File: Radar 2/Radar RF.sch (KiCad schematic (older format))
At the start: 140 parts, among them U10 Check_Point, U11 Check_Point, U12 TLV172, U13 5400BL15B050E, U14 Check_Point, U15 LT6232, U16 Check_Point, U17 HMC431LP4, U18 TRF37A75, U19 PAT1220-C-6DB, U20 SKY65404, U21 TQP5523, U22 SMA_Connector, U23 MITERED_BEND, U24 Check_Point, U26 Check_Point, U27 PAT1220-C-6DB, U28 MITERED_BEND, U29 Directional_Coupler, U30 SMA_Connector, U34 Check_Point, U36 Check_Point, U42 MITERED_BEND, U43 MITERED_BEND, U44 MITERED_BEND, U46 Check_Point, U5 Check_Point, U6 SG-210STF, U7 5400BL15B050E, U8 ADF4158, U9 ADL5801

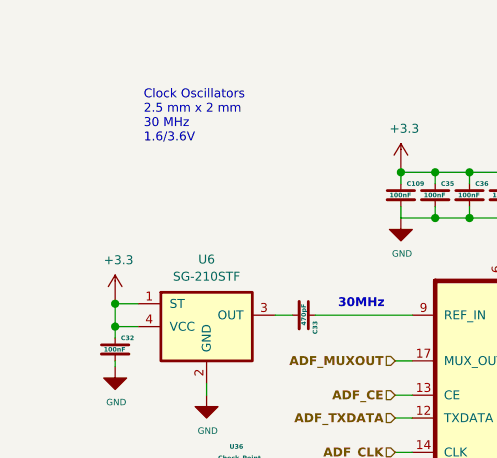
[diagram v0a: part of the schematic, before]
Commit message: Added datasheet for clock oscillator
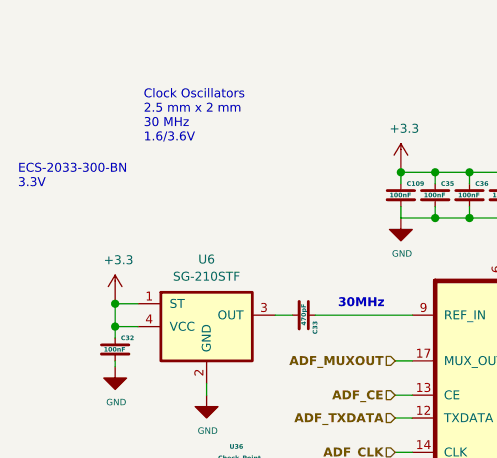
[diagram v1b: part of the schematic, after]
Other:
- note added: "ECS-2033-300-BN\n3.3V"
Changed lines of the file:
@@
 Text Notes 13500 1100 0    39   ~ 0
 CMX901QT8\nRF Amplifier 1W RF Power Amplifier\n130 MHz to 950 MHz\nGain 32dB\n6/2.5V\n
+Text Notes 750  1250 0    39   ~ 0
+ECS-2033-300-BN\n3.3V
 $EndSCHEMATC

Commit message: Minor changes in schematic
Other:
- note added: "Change this to 3 volt\nThis is tuning voltage"
- note added: "TLV172 not required as tunign volatge is upto 3 volt only"
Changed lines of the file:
@@
 Text Notes 750  1250 0    39   ~ 0
 ECS-2033-300-BN\n3.3V
+Text Notes 4350 1200 0    39   Italic 0
+Change this to 3 volt\nThis is tuning voltage
+Wire Notes Line
+	4350 1000 5050 1000
+Wire Notes Line
+	5050 1000 5050 1300
+Wire Notes Line
+	5050 1300 4350 1300
+Wire Notes Line
+	4350 1300 4350 1000
+Wire Notes Line
+	5150 900  7100 900
+Wire Notes Line
+	7100 900  7100 3000
+Wire Notes Line
+	7100 3000 5200 3000
+Wire Notes Line
+	5200 3000 5200 900
+Text Notes 5250 850  0    39   ~ 0
+TLV172 not required as tunign volatge is upto 3 volt only
+Wire Notes Line
+	9900 1900 10750 1900
+Wire Notes Line
+	10750 1900 10750 3200
+Wire Notes Line
+	10750 3200 9900 3200
+Wire Notes Line
+	9900 3200 9900 1900
+Wire Notes Line
+	7550 1550 8400 1550
+Wire Notes Line
+	8400 1550 8400 2500
+Wire Notes Line
+	8400 2500 7550 2500
+Wire Notes Line
+	7550 2500 7550 1550
+Wire Notes Line
+	11200 1700 12650 1700
+Wire Notes Line
+	12650 1700 12650 3050
+Wire Notes Line
+	12650 3050 11200 3050
+Wire Notes Line
+	11200 3050 11200 1700
+Wire Notes Line
+	11050 5400 12000 5400
+Wire Notes Line
+	12000 5400 12000 6350
+Wire Notes Line
+	12000 6350 11050 6350
+Wire Notes Line
+	11050 6350 11050 5400
+Wire Notes Line
+	7800 5700 8500 5700
+Wire Notes Line
+	8500 5700 8500 6400
+Wire Notes Line
+	8500 6400 7800 6400
+Wire Notes Line
+	7800 6400 7800 5700
+Wire Notes Line
+	2500 5600 3250 5600
+Wire Notes Line
+	3250 5600 3250 6350
+Wire Notes Line
+	3250 6350 2500 6350
+Wire Notes Line
+	2500 6350 2500 5600
 $EndSCHEMATC

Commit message: Modified for SubGHz. Added all datasheet for reference.
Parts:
- removed C59, C85, C87, C88: 100nF, Footprints:SMD_0402, symbol Radar-v2-rescue:Capacitor-Capacitor-Radar-RF-rescue-Radar-v2-rescue
- removed C82, C90: 1nF, Footprints:SMD_0402, symbol Radar-v2-rescue:Capacitor-Capacitor-Radar-RF-rescue-Radar-v2-rescue
- removed C89: 10uF, Footprints:SMD_0603, symbol Radar-v2-rescue:Capacitor-Capacitor-Radar-RF-rescue-Radar-v2-rescue
- removed L8: BLM18PG181SN1D, Footprints:SMD_0603, symbol Radar-v2-rescue:Ferrite_Bead-Ferrite_Bead-Radar-RF-rescue-Radar-v2-rescue
- removed R35: 0, Footprints:SMD_0402, symbol Radar-v2-rescue:Resistor-Resistor-Radar-RF-rescue-Radar-v2-rescue
- removed R36, R37: 4.7K, Footprints:SMD_0402, symbol Radar-v2-rescue:Resistor-Resistor-Radar-RF-rescue-Radar-v2-rescue
- removed R38: 100K, Footprints:SMD_0402, symbol Radar-v2-rescue:Resistor-Resistor-Radar-RF-rescue-Radar-v2-rescue
- removed R56: 1K, Footprints:SMD_0402, symbol Radar-v2-rescue:Resistor-Resistor-Radar-RF-rescue-Radar-v2-rescue
- removed R57: 0 to 27, Footprints:SMD_0402, symbol Radar-v2-rescue:Resistor-Resistor-Radar-RF-rescue-Radar-v2-rescue
- removed R58: 30K, Footprints:SMD_0402, symbol Radar-v2-rescue:Resistor-Resistor-Radar-RF-rescue-Radar-v2-rescue
- removed R75: DNP, Footprints:SMD_0402, symbol Radar-v2-rescue:Resistor-Resistor-Radar-RF-rescue-Radar-v2-rescue
- removed R76: 100, Footprints:SMD_0402, symbol Radar-v2-rescue:Resistor-Resistor-Radar-RF-rescue-Radar-v2-rescue
- removed U11, U24: Check_Point, Footprints:SolderPad_1_1.5mm_SMD_Circle, symbol Radar-v2-rescue:SolderPad_1_Circle-SolderPad_1_Circle
- removed U12: TLV172, Footprints:SC70_5, symbol Radar-v2-rescue:TLV172-TLV172-Radar-RF-rescue-Radar-v2-rescue
- removed U13, U7: 5400BL15B050E, Footprints:Balun_5400BL15B050E, symbol Radar-v2-rescue:5400BL15B050E-Balun-Radar-RF-rescue-Radar-v2-rescue
- removed U19: PAT1220-C-6DB, Footprints:PAT1220_6dB, symbol Radar-v2-rescue:ATTENUATOR_3Pin-ATTENUATOR_3Pin-Radar-RF-rescue-Radar-v2-rescue
- removed U20: SKY65404, Footprints:SKY65404_31, symbol Radar-v2-rescue:SKY65404-SKY65404-Radar-RF-rescue-Radar-v2-rescue
- removed U21: TQP5523, Footprints:QFN20_4x4mm_P0.5mm_1EXP_2.5x2.5mm, symbol Radar-v2-rescue:TQP5523-TQP5523-Radar-RF-rescue-Radar-v2-rescue
- added C? (x7): DNP, Footprints:SMD_0402, symbol Radar-v2-rescue:Capacitor-Capacitor-Radar-RF-rescue-Radar-v2-rescue
- added C? (x3): 1uF, Footprints:SMD_0402, symbol Radar-v2-rescue:Capacitor-Capacitor-Radar-RF-rescue-Radar-v2-rescue
- added C?: 4.7uF, Footprints:SMD_0402, symbol Radar-v2-rescue:Capacitor-Capacitor-Radar-RF-rescue-Radar-v2-rescue
- added C? (x2): 10nF, Footprints:SMD_0402, symbol Radar-v2-rescue:Capacitor-Capacitor-Radar-RF-rescue-Radar-v2-rescue
- added C?: 100pF, Footprints:SMD_0402, symbol Radar-v2-rescue:Capacitor-Capacitor-Radar-RF-rescue-Radar-v2-rescue
- added C?: 4.7pF, Footprints:SMD_0402, symbol Radar-v2-rescue:Capacitor-Capacitor-Radar-RF-rescue-Radar-v2-rescue
- added C?: 18pF, Footprints:SMD_0402, symbol Radar-v2-rescue:Capacitor-Capacitor-Radar-RF-rescue-Radar-v2-rescue
- added C?: 5.6pF, Footprints:SMD_0402, symbol Radar-v2-rescue:Capacitor-Capacitor-Radar-RF-rescue-Radar-v2-rescue
- added C?: 1nF, Footprints:SMD_0402, symbol Radar-v2-rescue:Capacitor-Capacitor-Radar-RF-rescue-Radar-v2-rescue
- added L? (x2): 27nH, Footprints:SMD_0603, symbol Radar-v2-rescue:Ferrite_Bead-Ferrite_Bead-Radar-RF-rescue-Radar-v2-rescue
- added L?: 16nH, Footprints:SMD_0603, symbol Radar-v2-rescue:Ferrite_Bead-Ferrite_Bead-Radar-RF-rescue-Radar-v2-rescue
- added L?: 3.6nH, Footprints:SMD_0603, symbol Radar-v2-rescue:Ferrite_Bead-Ferrite_Bead-Radar-RF-rescue-Radar-v2-rescue
- added L?: 43nH, Footprints:SMD_0603, symbol Radar-v2-rescue:Ferrite_Bead-Ferrite_Bead-Radar-RF-rescue-Radar-v2-rescue
- added R? (x2): DNP, Footprints:SMD_0402, symbol Radar-v2-rescue:Resistor-Resistor-Radar-RF-rescue-Radar-v2-rescue
- added R? (x3): 68K, Footprints:SMD_0402, symbol Radar-v2-rescue:Resistor-Resistor-Radar-RF-rescue-Radar-v2-rescue
- added R?: 47K, Footprints:SMD_0402, symbol Radar-v2-rescue:Resistor-Resistor-Radar-RF-rescue-Radar-v2-rescue
- added R?: 100K, Footprints:SMD_0402, symbol Radar-v2-rescue:Resistor-Resistor-Radar-RF-rescue-Radar-v2-rescue
- added R?: 39K, Footprints:SMD_0402, symbol Radar-v2-rescue:Resistor-Resistor-Radar-RF-rescue-Radar-v2-rescue
- added R?: 470, Footprints:SMD_0402, symbol Radar-v2-rescue:Resistor-Resistor-Radar-RF-rescue-Radar-v2-rescue
- added R?: 51, Footprints:SMD_0402, symbol Radar-v2-rescue:Resistor-Resistor-Radar-RF-rescue-Radar-v2-rescue
- added U?: CMX901QT8, symbol Rf_library:CMX901QT8
- added U?: BGA729N6E6327XTSA1, symbol Rf_library:BGA729N6E6327XTSA1
- added U? (x2): DXW21HN5011BL, symbol Rf_library:DXW21HN5011BL
- C83: value 0.5pF -> 1nF
- U27: value PAT1220-C-6DB -> PAT1220-C-8DB-T5
- U6: value SG-210STF -> ECS-2033-300-BN
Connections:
- net labels added: VGS1, VGS2, VGS3
- net labels removed: +10, DAC_OUT1, DET_OUT
- wire segments 497 -> 564
- no-connect marks 4 -> 2
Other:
- note added: "-2dBm Output"
- note added: "-8dBm\n"
- note added: "@3.3 max 16mA"
- note added: "All components value\nadjusted for 435MHz"
- note added: "Attenuator\nLoss 8dB"
- note added: "CMX901QT8\nRF Amplifier 1W RF Power Amplifier\n130 MHz to 950 MHz\nGain 42dB @435MHz\n6/2.5V\n2.2Amp\n"
- note added: "Changed this to 3 volt\nThis is tuning voltage"
- note added: "LNA\nBGA729N6E6327XTSA1\nInsertion power gain: 16.3 dB\nOperating frequency: 70 - 1000 MHz\nSupply voltage: 1.5 V to 3.3 V\nRF input and output internally matched to 50 Ω"
- note added: "Max 0dBm\n-8dBm input"
- note added: "Max 2dBm input to LNA"
- note added: "Max Input Power: 10 dBm\nNF: 4.0 dB\nGain: 13 dB at 450MHz\nOIP3: 23 dBm\nOP1dB: 12 dBm\n"
- note added: "Max Input Power: 2dBm\nNF: 1.05dB\nGain: 16.3dB at 450MHz\nIIP3: -6 dBm\nIP1dB: -15 dBm"
- note added: "Pout -2dBm\n@3v, 27mA"
- note added: "Pout = 24 dB to 34 dB -16dB\n= 8dB-18dB\n"
- note added: "Pout = 32 to 42dBm - 8dB\n = 24 to 34 dBm\n"
- note added: "Pout = 8 to 18 dBm - 8dB\n = 0 to 10 dBm"
- note added: "TLV172 not required as \ntuning voltage is upto 0.5-3.0V only"
- note removed: "+2dBm Output"
- note removed: "-10dBm\n"
- note removed: "-4dBm\n"
- note removed: "100mW rating"
- note removed: "2.8 to 5.0 range"
- note removed: "29 to 37dB, typ. 32dB Gain\nOP1dB 31dBm\nPout = 22 to 27dBm\nPout = 21dBm 5V, 300mA"
- note removed: "@3.0 max 15mA"
- note removed: "Attenuator\nLoss 6dB"
- note removed: "CMX901QT8\nRF Amplifier 1W RF Power Amplifier\n130 MHz to 950 MHz\nGain 32dB\n6/2.5V\n"
- note removed: "Change this to 3 volt\nThis is tuning voltage"
- note removed: "Clock Oscillators\n2.5 mm x 2 mm\n30 MHz\n1.6/3.6V"
- note removed: "ECS-2033-300-BN\n3.3V"
- note removed: "If DAC will be used\nchange R35(0) with 4.7K to make gain 3"
- note removed: "LNA\n4.9 GHz to 5.9 GHz\n2.8/5V"
- note removed: "Low Noise Amplifiers\nBGU7032,115\n40 MHz to 1 GHz\nP1dB 14 dBm\nGain 10dB\n5V\nNF 4.5dB\n43mA\nOIP3 29dBm"
- note removed: "Max 0dBm\n-4dBm input"
- note removed: "Max 1dBm input to LNA"
- note removed: "Max Input Power: 10 dBm\nNF: 4.0 dB\nGain: 11 dB at 6 GHz\nOIP3: 23 dBm\nOP1dB: 12 dBm\n"
- note removed: "Max Input Power: 1dBm\nNF: 1dB\nGain: 12dB at 6GHz\nIIP3: 9 dBm\nIP1dB: -4 dBm"
- note removed: "PI Type Attenuator Network\n1 and 2 can be both in/out, directionless"
- note removed: "Pout 2dBm\n@3v, 27mA"
- note removed: "Pout = 22 to 27dBm - 16dB\n = 6 to 11 dBm\n"
- note removed: "Pout = 6 to 11 dBm - 6 dB\n = 0 to 5 dBm"
- note removed: "RC filter makes it noisy. \nI just placed 100K series resistor\nto filter noise."
- note removed: "SKY65017-70LF\nRF Amplifier\n100 MHz to 6 GHz\nP1dB 20dBm\nGain 20dB\n5V\nNF 4.5dB\nOIP3 35dBm"
- note removed: "Scale 3.3V DAC output to 10V"
- note removed: "Scale 5V PLL output to 10V"
- note removed: "TLV172 not required as tunign volatge is upto 3 volt only"
- note removed: "VCO Oscillators\n5.5 GHz to 6.1 GHz\n2.75/3.25V\n"
- moved on the sheet: C60, C61, C71, C72, C75, C76, C79, C80, C81, C83, C84, C86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
